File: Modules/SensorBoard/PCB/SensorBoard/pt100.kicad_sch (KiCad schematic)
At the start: 0 parts

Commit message: sensor board basic components
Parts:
- added J2: PT100_Ext, Connector_JST:JST_ZH_S3B-ZR-SM4A-TF_1x03-1MP_P1.50mm_Horizontal, symbol Connector_Generic:Conn_01x03
- added J3: PT100_Int, Connector_JST:JST_ZH_S3B-ZR-SM4A-TF_1x03-1MP_P1.50mm_Horizontal, symbol Connector_Generic:Conn_01x03
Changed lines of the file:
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@@
 (kicad_sch
-	(version 20231120)
+	(version 20250114)
 	(generator "eeschema")
-	(generator_version "8.0")
+	(generator_version "9.0")
 	(paper "A4")
+	(symbol
+		(lib_id "Connector_Generic:Conn_01x03")
+		(at 74.93 63.5 180)
+		(unit 1)
+		(exclude_from_sim no)
+		(in_bom yes)
+		(on_board yes)
+		(dnp no)
+		(fields_autoplaced yes)
+		(property "Reference" "J2"
+			(at 74.93 54.61 0)
+			(effects
+				(font
+					(size 1.27 1.27)
+				)
+			)
+		)
+		(property "Value" "PT100_Ext"
+			(at 74.93 57.15 0)
+			(effects
+				(font
+					(size 1.27 1.27)
+				)
+			)
+		)
+		(property "Footprint" "Connector_JST:JST_ZH_S3B-ZR-SM4A-TF_1x03-1MP_P1.50mm_Horizontal"
+			(at 74.93 63.5 0)
+			(effects
+				(font
+					(size 1.27 1.27)
+				)
+				(hide yes)
+			)
+		)
+		(property "Datasheet" "~"
+			(at 74.93 63.5 0)
+			(effects
+				(font
+					(size 1.27 1.27)
+				)
+				(hide yes)
+			)
+		)
+		(property "Description" "Generic connector, single row, 01x03, script generated (kicad-library-utils/schlib/autogen/connector/)"
+			(at 74.93 63.5 0)
+			(effects
+				(font
+					(size 1.27 1.27)
+				)
+				(hide yes)
+			)
+		)
+		(pin "2"
+		)
+		(pin "1"
+		)
+		(pin "3"
+		)
+		(instances
+			(project ""
+				(path "/fa219048-dcb4-48ee-a6b6-8b1fad43a054/3b7a1f5d-723d-48a0-b5b1-eb6f60cd6fcc"
+					(reference "J2")
+					(unit 1)
+				)
+			)
+		)
+	)
+	(symbol
+		(lib_id "Connector_Generic:Conn_01x03")
+		(at 74.93 88.9 180)
+		(unit 1)
+		(exclude_from_sim no)
+		(in_bom yes)
+		(on_board yes)
+		(dnp no)
+		(fields_autoplaced yes)
+		(property "Reference" "J3"
+			(at 74.93 80.01 0)
+			(effects
+				(font
+					(size 1.27 1.27)
+				)
+			)
+		)
+		(property "Value" "PT100_Int"
+			(at 74.93 82.55 0)
+			(effects
+				(font
+					(size 1.27 1.27)
+				)
+			)
+		)
+		(property "Footprint" "Connector_JST:JST_ZH_S3B-ZR-SM4A-TF_1x03-1MP_P1.50mm_Horizontal"
+			(at 74.93 88.9 0)
+			(effects
+				(font
+					(size 1.27 1.27)
+				)
+				(hide yes)
+			)
+		)
+		(property "Datasheet" "~"
+			(at 74.93 88.9 0)
+			(effects
+				(font
+					(size 1.27 1.27)
+				)
+				(hide yes)
+			)
+		)
+		(property "Description" "Generic connector, single row, 01x03, script generated (kicad-library-utils/schlib/autogen/connector/)"
+			(at 74.93 88.9 0)
+			(effects
+				(font
+					(size 1.27 1.27)
+				)
+				(hide yes)
+			)
+		)
+		(pin "2"
+		)
+		(pin "1"
+		)
+		(pin "3"
+		)
+		(instances
+			(project "SensorBoard"
+				(path "/fa219048-dcb4-48ee-a6b6-8b1fad43a054/3b7a1f5d-723d-48a0-b5b1-eb6f60cd6fcc"
+					(reference "J3")
+					(unit 1)
+				)
+			)
+		)
+	)
 )

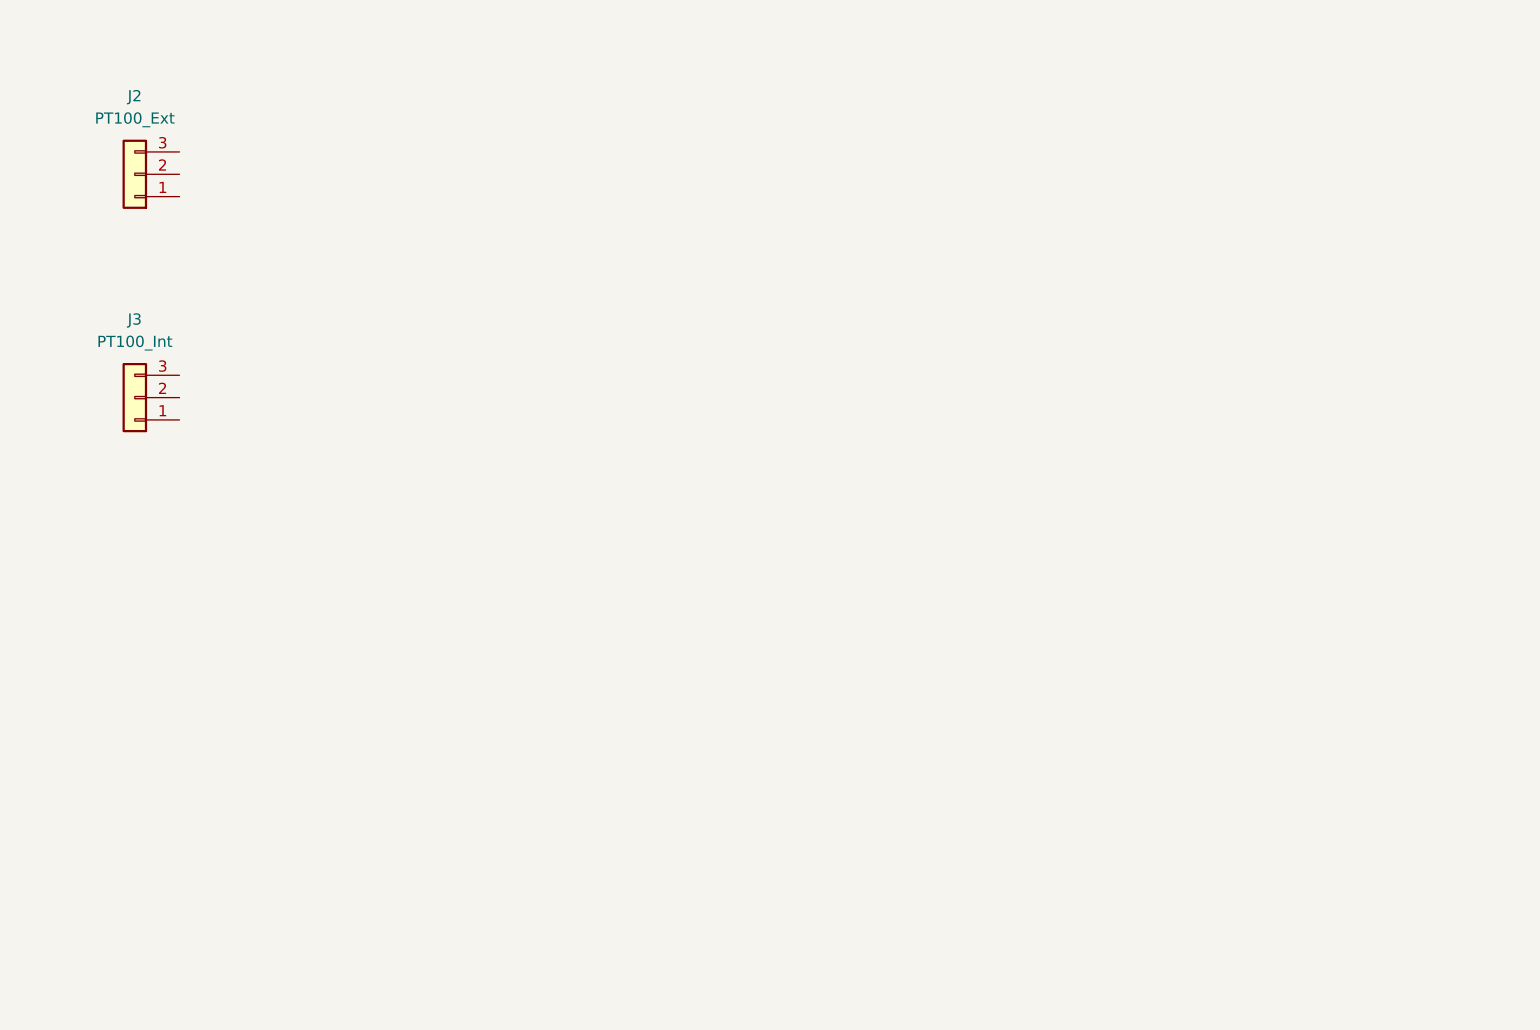
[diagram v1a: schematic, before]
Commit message: Enrutado de diseño de PT100 en la sensorboard
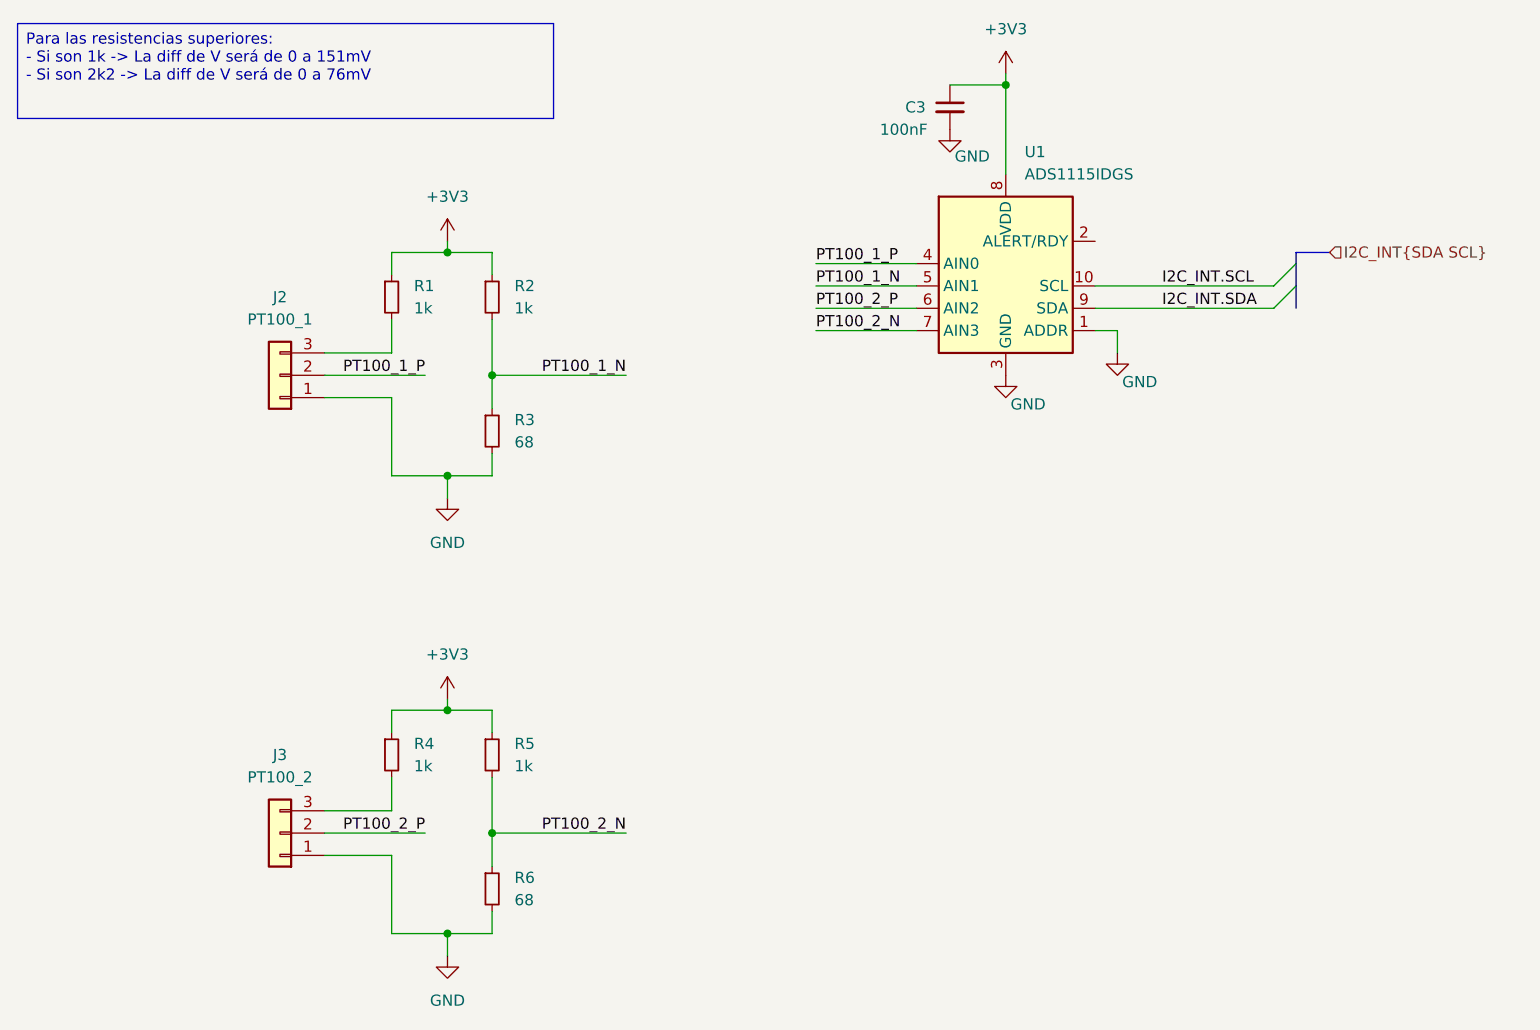
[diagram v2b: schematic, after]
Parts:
- added C3: 100nF, Capacitor_SMD:C_0603_1608Metric_Pad1.08x0.95mm_HandSolder, symbol Device:C_Small
- added R1, R2, R4, R5: 1k, Resistor_SMD:R_0805_2012Metric_Pad1.20x1.40mm_HandSolder, symbol Device:R_Small
- added R3, R6: 68, Resistor_SMD:R_0805_2012Metric_Pad1.20x1.40mm_HandSolder, symbol Device:R_Small
- added U1: ADS1115IDGS, Package_SO:TSSOP-10_3x3mm_P0.5mm, symbol Analog_ADC:ADS1115IDGS
- J2: value PT100_Ext -> PT100_1
- J3: value PT100_Int -> PT100_2
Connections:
- net GND: now reaches J2.1 (Pin_1)
- net GND: now also J3.1 (Pin_1), C3.2, R3.2, R6.2, U1.1 (ADDR), U1.3 (GND)
- net PT100_1_P: now reaches J2.2 (Pin_2)
- net PT100_1_P: now also U1.4 (AIN0)
- net at J2.3 (Pin_3): now also R1.2
- net PT100_2_P: now reaches J3.2 (Pin_2)
- net PT100_2_P: now also U1.6 (AIN2)
- net at J3.3 (Pin_3): now also R4.2
- new net +3V3: C3.1, R1.1, R2.1, R4.1, R5.1, U1.8 (VDD)
- new net I2C_INT.SCL: U1.10 (SCL)
- new net I2C_INT.SDA: U1.9 (SDA)
- new net PT100_1_N: R2.2, R3.1, U1.5 (AIN1)
- new net PT100_2_N: R5.2, R6.1, U1.7 (AIN3)
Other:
- moved on the sheet: J2, J3
